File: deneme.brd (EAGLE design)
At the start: 100 x 80 mm, 26 parts, among them Q2 BCX70SMD, Q3 BCX70SMD, Q4 BCX70SMD, Q5 BCX70SMD, Q6 BCX70SMD, Q7 BCX70SMD, Q8 BCX70SMD, Q9 BCX70SMD

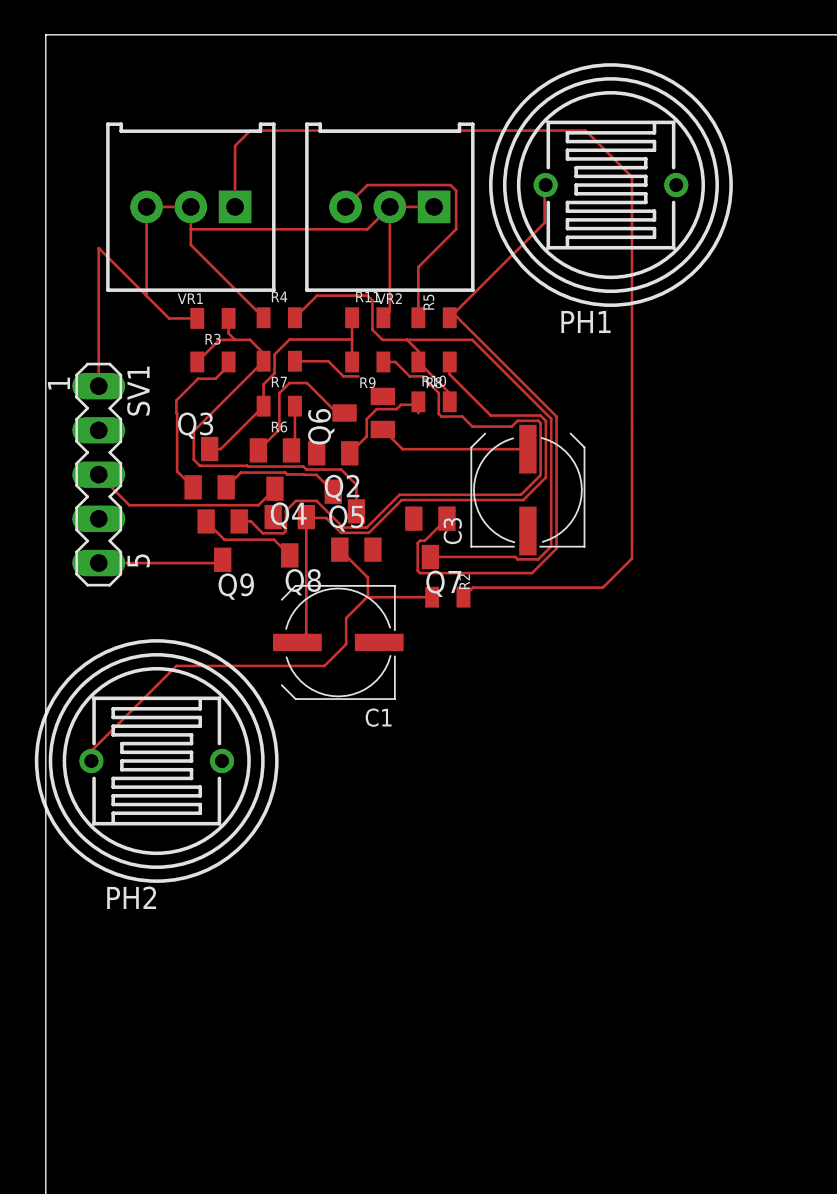
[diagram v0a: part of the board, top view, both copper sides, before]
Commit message: Ldr changed, curcuit was drawn  from the beginning
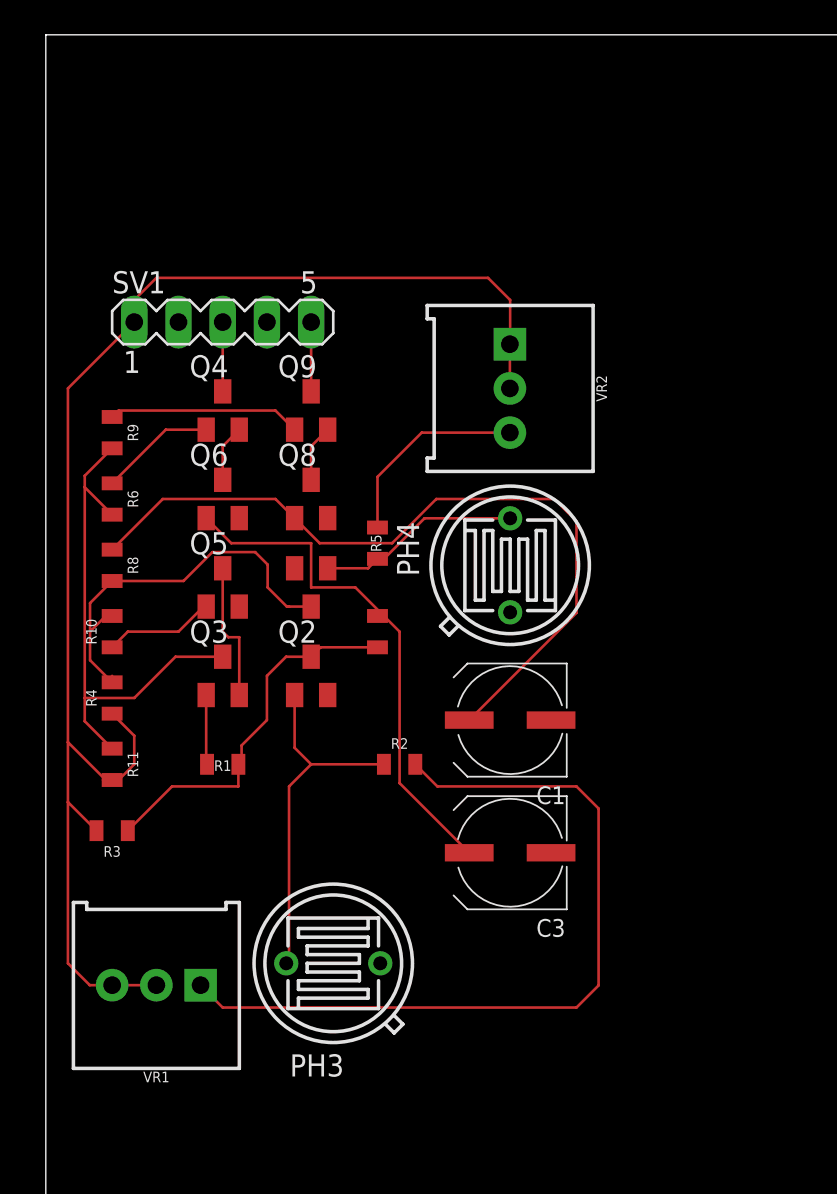
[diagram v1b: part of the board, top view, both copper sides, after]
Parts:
- removed PH1, PH2: B1060_23, photo-elements:TO-8_B10
- added PH3, PH4: V1060_31, photo-elements:TO-5_V10
- moved VR1 44.7 mm to (6.35, 25.4)
- moved R3 30.0 mm to (3.81, 34.3)
- moved R11 29.6 mm to (3.81, 38.1), turned to 270 degrees
- moved R4 23.9 mm to (3.81, 41.9), turned to 90 degrees
- moved R1 23.1 mm to (10.2, 38.1), turned to 0 degrees
- moved R10 22.7 mm to (3.81, 45.7), turned to 90 degrees
- moved R8 21.9 mm to (3.81, 49.5), turned to 270 degrees
- moved C3 20.9 mm to (26.7, 33.0), turned to 180 degrees
- moved R7 16.5 mm to (19.1, 45.7), turned to 270 degrees
- moved R9 15.2 mm to (3.81, 57.1), turned to 270 degrees
- moved R5 13.4 mm to (19.1, 50.8), turned to 270 degrees
- moved VR2 12.5 mm to (26.7, 59.7), turned to 270 degrees
- moved Q3 12.0 mm to (10.2, 43.2)
- moved SV1 11.3 mm to (10.2, 63.5), turned to 0 degrees
- moved R6 11.0 mm to (3.81, 53.3), turned to 270 degrees
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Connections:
- net GND: now also PH3.2, PH4.2; no longer PH1.2, PH2.2
- net N$4: now also PH3.1; no longer PH2.1
- net N$6: now also PH4.1; no longer PH1.1
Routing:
- net VCC: track 52.1 -> 84.4 mm
- net N$6: track 38.9 -> 11.7 mm
- net N$21: track 35.4 -> 11.1 mm
- net N$3: track 13.7 -> 30.0 mm
- net N$13: track 15.0 -> 30.1 mm
- net N$9: track 38.4 -> 23.4 mm
- net N$1: track 60.5 -> 45.7 mm
- net N$19: track 33.4 -> 45.2 mm
- net M_VCC: track 11.2 -> 3.98 mm
- net N$4: track 28.1 -> 20.9 mm
- net N$12: track 9.43 -> 4.00 mm
- net N$15: track 8.48 -> 3.27 mm
- net N$5: track 2.62 -> 6.68 mm
- net N$14: track 25.3 -> 21.5 mm
- net N$7: track 15.2 -> 11.6 mm
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
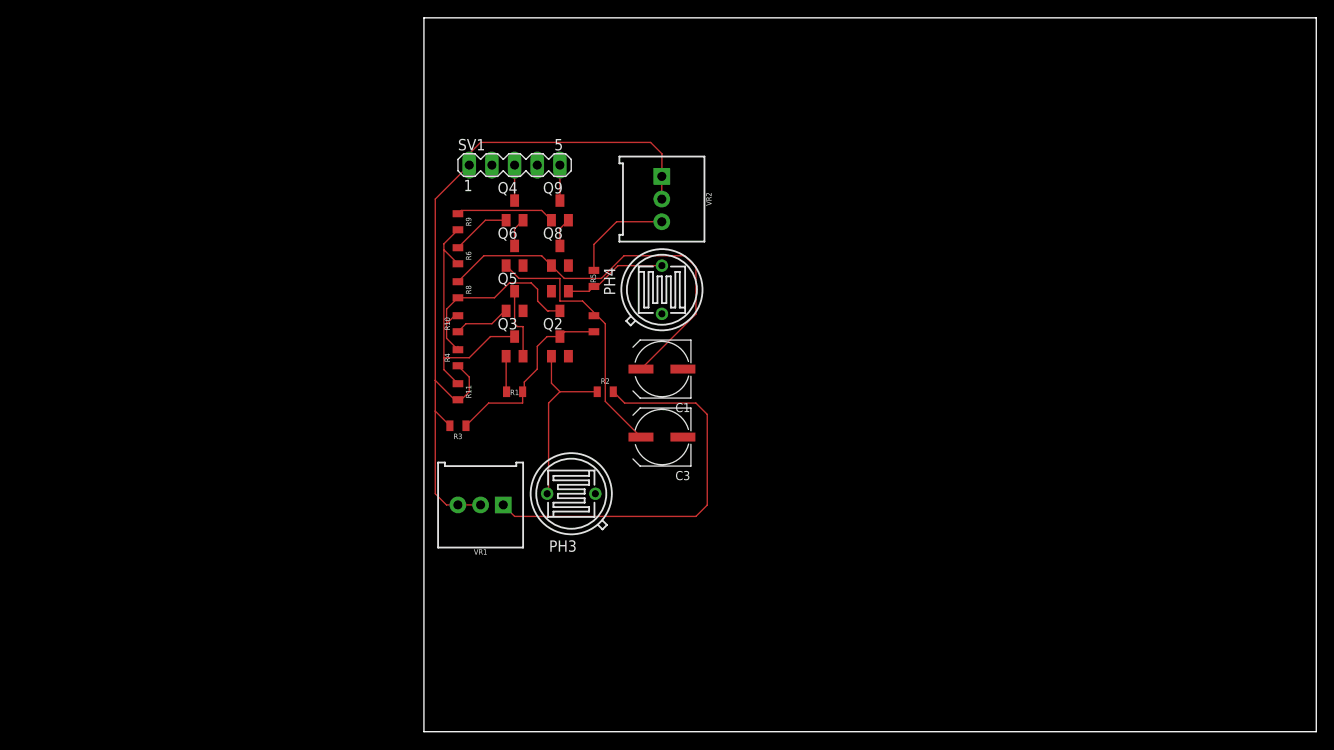
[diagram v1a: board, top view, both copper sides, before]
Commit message: project finished
pot and ldr changed.  Shortcomings completed.
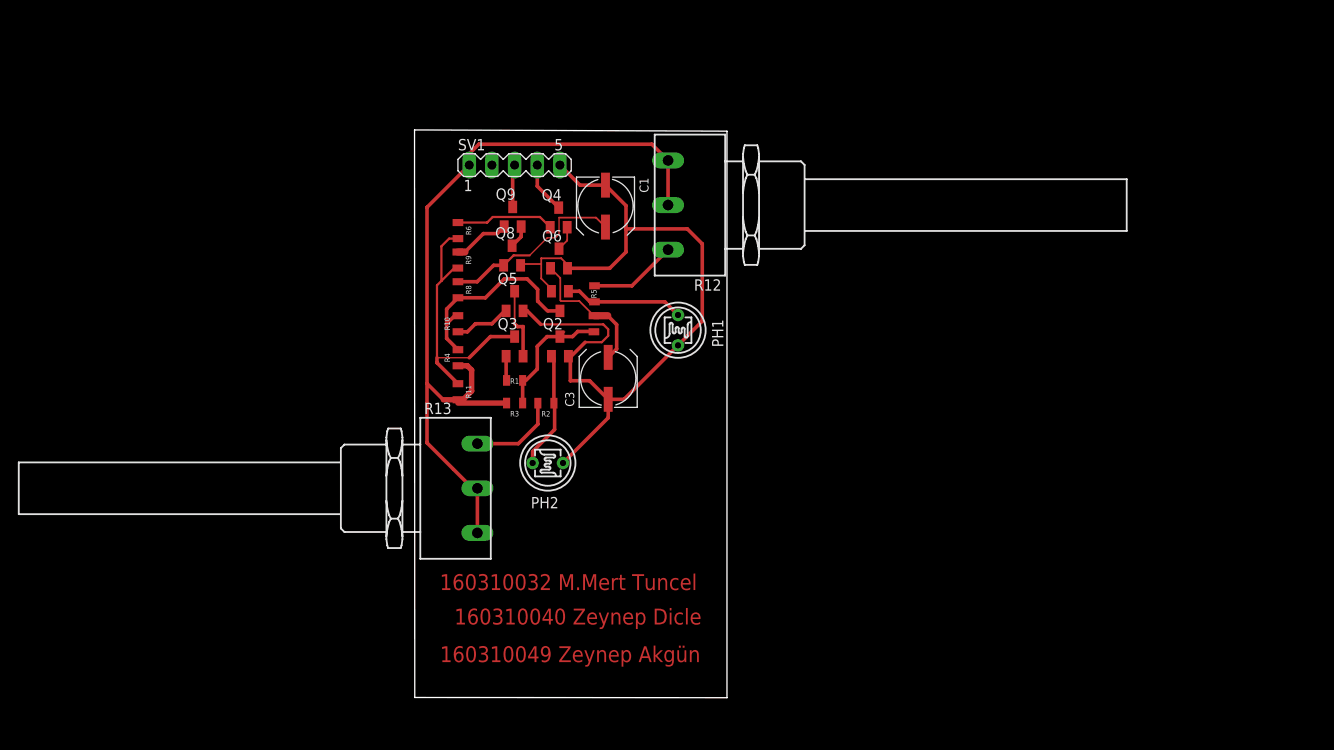
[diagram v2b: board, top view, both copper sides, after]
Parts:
- removed PH3, PH4: V1060_31, photo-elements:TO-5_V10
- removed VR1, VR2: 10k, SparkFun-Resistors:TRIMPOT-PTH-3386U
- added PH1, PH2: A1050_12, photo-elements:T0-46-A10XX
- added R12, R13: PC16S, piher:PC16S
- moved C1 19.3 mm to (20.3, 58.9), turned to 270 degrees
- moved C3 8.92 mm to (20.7, 39.6), turned to 90 degrees
- moved R3 6.84 mm to (10.2, 36.8)
- moved R2 6.78 mm to (13.7, 36.8), turned to 180 degrees
- moved Q8 5.36 mm to (9.88, 53.4)
- moved Q9 5.34 mm to (9.94, 57.7)
- moved Q4 5.00 mm to (15.1, 57.6)
- moved Q6 4.99 mm to (15.1, 53.0)
- moved R9 4.29 mm to (3.80, 52.9)
- moved R6 2.82 mm to (3.81, 56.2)
- moved R5 1.73 mm to (19.1, 49.1)
- moved R1 1.27 mm to (10.2, 39.4)
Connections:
- net GND: now also PH1.1, PH2.2, SV1.5; no longer PH3.2, PH4.2, SV1.2
- net M_VCC: now also SV1.4; no longer SV1.3
- net M_VCC2: now also SV1.3; no longer SV1.5
- net N$1: now also R13.1A; no longer VR1.1
- net N$4: now also PH2.1; no longer PH3.1
- net N$6: now also PH1.2; no longer PH4.1
- net N$7: now also R12.1A; no longer VR2.3
- net VCC: now also R12.1E, R12.1S, R13.1E, R13.1S; no longer VR1.2, VR1.3, VR2.1, VR2.2
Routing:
- net GND: track 0.00 -> 97.8 mm
- net N$1: track 45.7 -> 10.0 mm
- net N$19: track 45.2 -> 21.5 mm
- net VCC: track 84.4 -> 101.2 mm
- net N$3: track 30.0 -> 16.2 mm
- net N$4: track 20.9 -> 13.4 mm
- net N$14: track 21.5 -> 15.1 mm
- net N$21: track 11.1 -> 6.38 mm
- net N$5: track 6.68 -> 11.1 mm
- net M_VCC: track 3.98 -> 5.76 mm
- net N$6: track 11.7 -> 13.4 mm
- net N$7: track 11.6 -> 9.92 mm
- net N$12: track 4.00 -> 2.73 mm
- net N$13: track 30.1 -> 31.3 mm
- net M_VCC2: track 3.98 -> 4.78 mm
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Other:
- board size 100 x 80 mm -> 35 x 63.6 mm
- board text added: "160310032 M.Mert Tuncel"
- board text added: "160310040 Zeynep Dicle"
- board text added: "160310049 Zeynep Akgün"
